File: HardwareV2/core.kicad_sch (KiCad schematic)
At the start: 4 parts, among them SW6 1825910-6, SW7 1825910-6

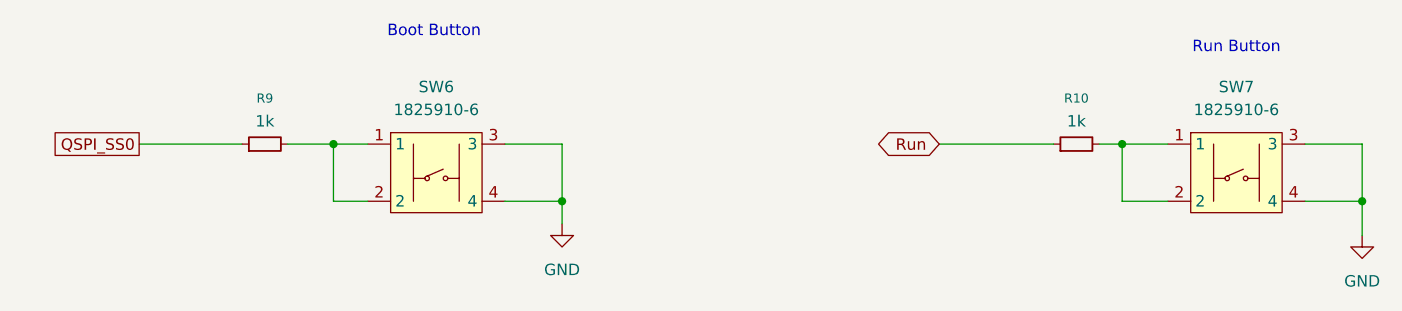
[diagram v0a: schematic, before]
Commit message: initial v2 pcb layout minus passives
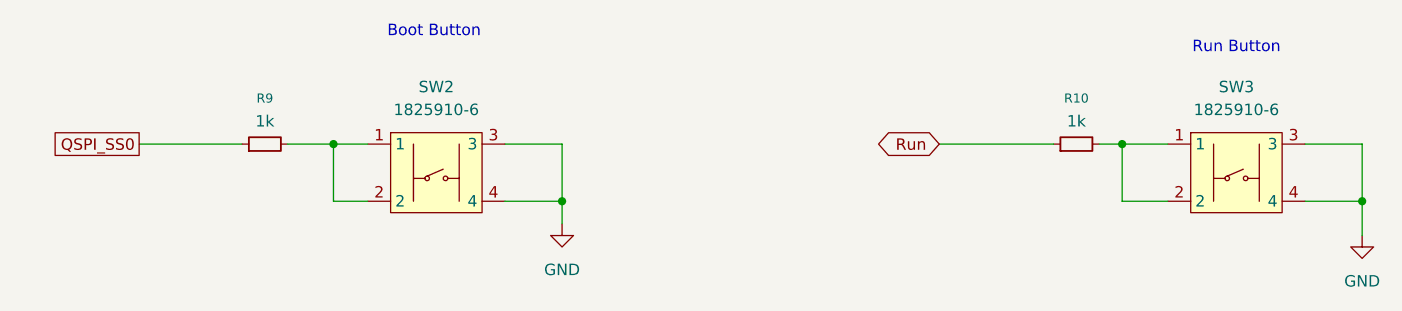
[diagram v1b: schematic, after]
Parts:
- R10, R9: footprint (none) -> Resistor_SMD:R_0805_2012Metric
- SW2: renamed from SW6; footprint parts_lib:SW-TH_4P-L6.0-W6.0-P4.50-LS6.5 -> RP2350b_parts_layout:SW-TH_4P-L6.0-W6.0-P4.50-LS6.5
- SW3: renamed from SW7; footprint parts_lib:SW-TH_4P-L6.0-W6.0-P4.50-LS6.5 -> RP2350b_parts_layout:SW-TH_4P-L6.0-W6.0-P4.50-LS6.5
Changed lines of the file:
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@@
 			)
 		)
-		(property "Footprint" ""
+		(property "Footprint" "Resistor_SMD:R_0805_2012Metric"
 			(at 83.82 40.64 0)
 			(effects
@@
 		(dnp no)
 		(fields_autoplaced yes)
-		(property "Reference" "SW6"
+		(property "Reference" "SW2"
 			(at 102.87 34.29 0)
 			(effects
@@
 			)
 		)
-		(property "Footprint" "parts_lib:SW-TH_4P-L6.0-W6.0-P4.50-LS6.5"
+		(property "Footprint" "RP2350b_parts_layout:SW-TH_4P-L6.0-W6.0-P4.50-LS6.5"
 			(at 102.616 53.34 0)
 			(effects
@@
 			(project "RP2350b_Console_v2"
 				(path "/72e8720b-5adf-4b6d-9b96-dda4c7035d94/89d4dab2-66d8-4149-a2b3-9fe3e528e793"
-					(reference "SW6")
+					(reference "SW2")
 					(unit 1)
 				)
@@
 		(dnp no)
 		(fields_autoplaced yes)
-		(property "Reference" "SW7"
+		(property "Reference" "SW3"
 			(at 191.77 34.29 0)
 			(effects
@@
 			)
 		)
-		(property "Footprint" "parts_lib:SW-TH_4P-L6.0-W6.0-P4.50-LS6.5"
+		(property "Footprint" "RP2350b_parts_layout:SW-TH_4P-L6.0-W6.0-P4.50-LS6.5"
 			(at 191.516 53.34 0)
 			(effects
@@
 			(project "RP2350b_Console_v2"
 				(path "/72e8720b-5adf-4b6d-9b96-dda4c7035d94/89d4dab2-66d8-4149-a2b3-9fe3e528e793"
-					(reference "SW7")
+					(reference "SW3")
 					(unit 1)
 				)
@@
 			)
 		)
-		(property "Footprint" ""
+		(property "Footprint" "Resistor_SMD:R_0805_2012Metric"
 			(at 173.99 40.64 0)
 			(effects
